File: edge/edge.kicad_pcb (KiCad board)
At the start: 2 copper layers, 50 x 50 mm, 22 parts, among them IC1 ATTINY861A-S, P1 CONN_6, P2 CONN_6, P3 CONN_5, P4 CONN_6, P5 CONN_3X2, Q1 MOSFET_N, Q2 MOSFET_N, Q3 MOSFET_N

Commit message: Last version before ATtiny24A
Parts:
- added R4: 10K, SM0603, F.Cu at (215.5, 112.5)
- added R5: 10K, SM0603, F.Cu at (217.5, 112.5)
- moved C5 20.2 mm to (211.0, 122.0), turned to 270 degrees
- moved C6 19.4 mm to (212.0, 115.0), turned to 90 degrees
- moved C8 17.5 mm to (212.0, 119.0), turned to 270 degrees
- moved P3 17.0 mm to (208.0, 141.0), turned to 90 degrees
- moved Q3 16.5 mm to (213.0, 130.0)
- moved R3 16.1 mm to (213.0, 127.0), turned to 0 degrees
- moved C2 15.7 mm to (219.5, 114.5), turned to 90 degrees
- moved C9 13.5 mm to (238.0, 107.0), turned to 90 degrees
- moved P4 13.3 mm to (229.5, 122.5), turned to 180 degrees
- moved P5 11.1 mm to (236.2, 121.0), turned to 90 degrees
- moved C4 10.3 mm to (221.5, 125.0)
- moved P1 10.0 mm to (208.0, 113.0)
- moved P2 10.0 mm to (242.0, 113.0)
- moved Q1 8.06 mm to (228.0, 130.0)
- moved C7 7.81 mm to (238.0, 111.0), turned to 270 degrees
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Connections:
- C3 pad 2: N-000007 (its old number) -> /OUT
- IC1 pad 1: /OUT -> /MOSI
- IC1 pad 19: N-0000019 (its old number) -> /BTN2
- IC1 pad 2: /RED -> /BLUE
- IC1 pad 20: /PA0 -> /BTN1
- IC1 pad 3: N-000004 -> /PB2
- IC1 pad 7: N-000005 -> /PB4
- IC1 pad 8: /BLUE -> /RED
- L1 pad 1: /OUT -> /MOSI
- L1 pad 2: N-000007 (its old number) -> /OUT
- P4 pad 5: /PA0 -> /PB2
- P4 pad 6: /PA2 -> /PB4
- P5 pad 1: /MISO -> /BLUE
- P5 pad 3: /SCK -> /PB2
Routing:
- net +3.3V: track 0.00 -> 101.2 mm, vias 0 -> 6
- net +12V: track 0.00 -> 93.2 mm, vias 0 -> 2
- net /OUT: track 0.00 -> 50.1 mm
- net N-000001: track 0.00 -> 35.6 mm
- net GND: track 0.00 -> 31.6 mm, vias 0 -> 12
- net /INCCW2: track 0.00 -> 25.6 mm, vias 0 -> 2
- net /INCW2: track 0.00 -> 24.6 mm
- net N-0000018: track 0.00 -> 22.4 mm
- net /\RESET: track 0.00 -> 21.6 mm
- net /INCCW1: track 0.00 -> 16.4 mm
- net /INCW1: track 0.00 -> 16.1 mm
- net N-0000019: track 0.00 -> 10.9 mm
- net /BLUE: track 0.00 -> 10.2 mm
- net /PB2: track 0.00 -> 10.1 mm
- net /PB4: track 0.00 -> 8.33 mm
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- added copper zone on F.Cu, net /BTN1C
- added copper zone on F.Cu, net /BTN2C
- added copper zone on B.Cu, net GND
- added copper zone on F.Cu, net GND
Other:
- net class Default: clearance 0.254 -> 0.2032; trace_width 0.254 -> 0.2032; via_dia 0.889 -> 0.6096; via_drill 0.635 -> 0.3048
- net class hipower added: clearance 0.3048, trace_width 0.508, via_dia 1.27, via_drill 0.762
- net class power added: clearance 0.2032, trace_width 0.3048, via_dia 0.889, via_drill 0.508
- rule trace_clearance: 0.254 -> 0.2032
- rule trace_min: 0.254 -> 0.1524
- rule via_min_drill: 0.508 -> 0.3048
- rule via_min_size: 0.889 -> 0.6096

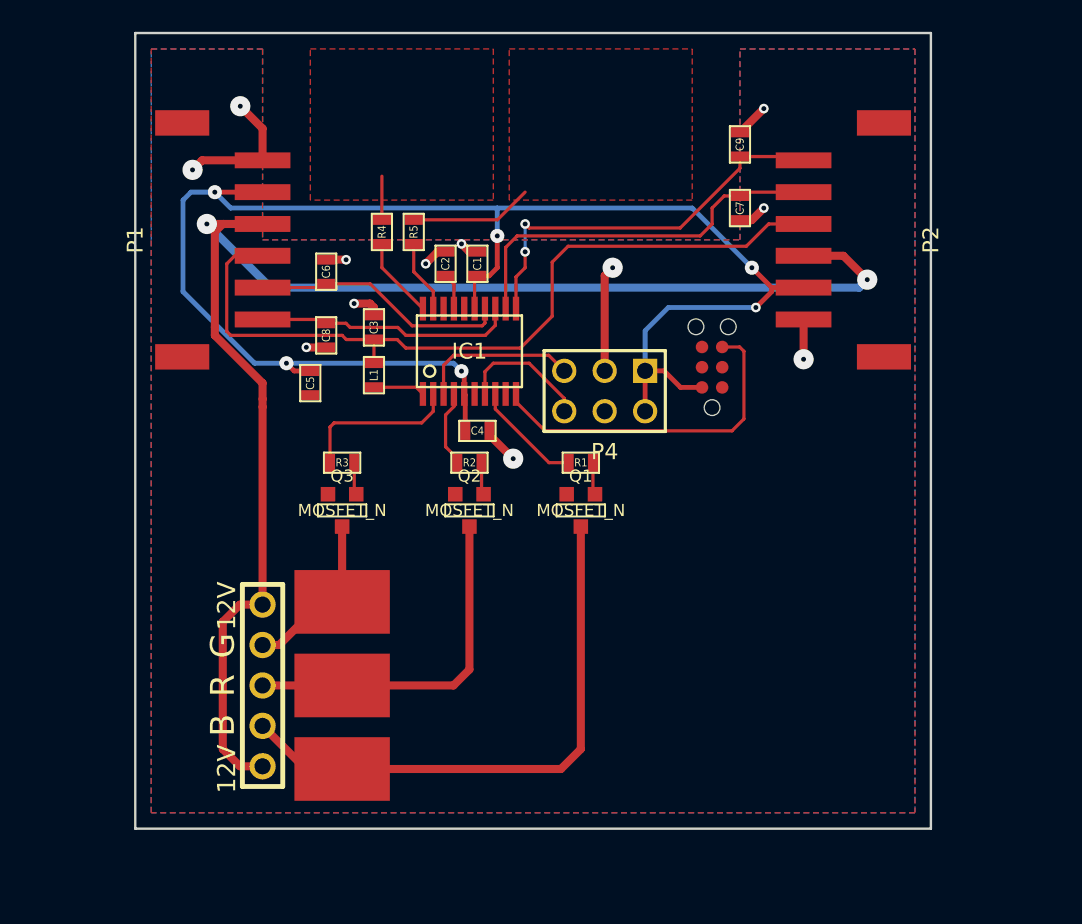
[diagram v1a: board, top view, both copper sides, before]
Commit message: ATtiny24A based edge board
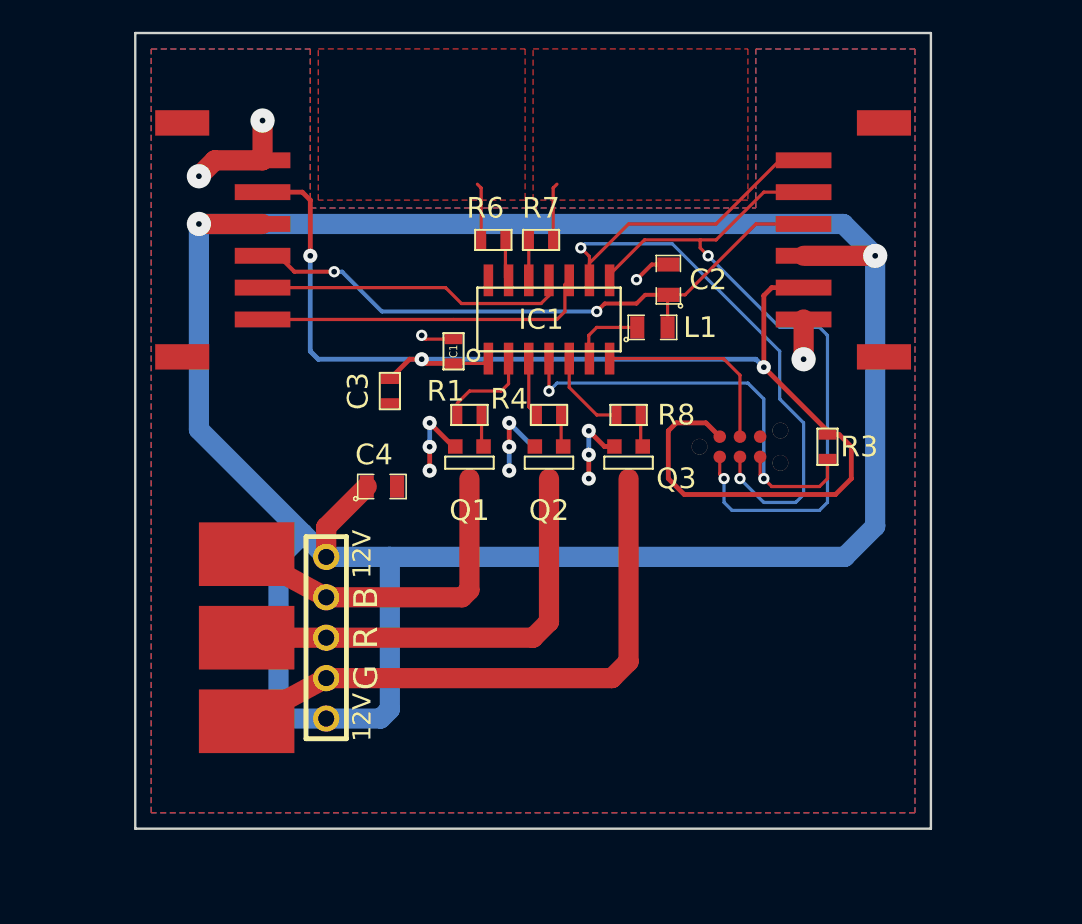
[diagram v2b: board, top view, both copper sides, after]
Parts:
- removed C5: 2.2uF, SM0603
- removed C6, C7, C8, C9: 0.1uF, SM0603
- removed P4: CONN_6, pin_array_3x2
- removed R2: 22R, SM0603
- removed R5: 10K, SM0603
- added R6: 10K, SM0603, F.Cu at (222.5, 113.0)
- added R7: 10K, SM0603, F.Cu at (225.5, 113.0)
- added R8: 170R, SM0603, F.Cu at (231.0, 124.0)
- C2, C4: value 0.1uF -> 10uF; footprint SM0603 -> SM0805
- C3: value 0.1uF -> 1uF
- IC1: value ATTINY861A-S -> ATTINY24A-SS; footprint TSSOP20-4.5MM -> SOIC14-4MM
- L1: footprint SM0603 -> SM0805
- Q1, Q2, Q3: value MOSFET_N -> NPN; footprint SOT23GDS -> SOT23EBC
- R1: value 22R -> 170R
- R3: value 22R -> 10K
- R4: value 10K -> 170R
- moved R3 30.5 mm to (243.5, 126.0), turned to 90 degrees
- moved Q3 18.2 mm to (231.0, 127.0)
- moved L1 17.8 mm to (232.5, 118.5), turned to 0 degrees
- moved R4 15.6 mm to (226.0, 124.0), turned to 0 degrees
- moved C2 14.0 mm to (233.5, 115.5)
- moved Q1 7.62 mm to (221.0, 127.0)
- moved R1 7.62 mm to (221.0, 124.0)
- moved C4 6.95 mm to (215.5, 128.5), turned to 0 degrees
- moved Q2 5.83 mm to (226.0, 127.0)
- moved C1 5.70 mm to (220.0, 120.0), turned to 270 degrees
- moved IC1 5.39 mm to (226.0, 118.0)
- moved P5 5.30 mm to (238.0, 126.0), turned to 0 degrees
- moved P3 5.00 mm to (212.0, 138.0), turned to 270 degrees
- moved C3 4.12 mm to (216.0, 122.5)
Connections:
- C1 pad 1: +3.3V -> GND
- C1 pad 2: GND -> +3.3V
- C2 pad 1: N-000006 -> /OUT
- C3 pad 1: GND -> +3.3V
- C3 pad 2: /OUT -> GND
- C4 pad 1: GND -> +12V
- C4 pad 2: +3.3V -> GND
- IC1 pad 1: /MOSI -> +3.3V
- IC1 pad 10: /\RESET -> /INCCW1
- IC1 pad 11: /INCCW2 -> /INCW1
- IC1 pad 12: /INCW2 -> /BTN2
- IC1 pad 13: /INCCW1 -> /BTN1
- IC1 pad 14: /INCW1 -> GND
- IC1 pad 2: /BLUE -> /RED
- IC1 pad 3: /PB2 -> /GREEN
- IC1 pad 4: /GREEN -> /\RESET
- IC1 pad 5: +3.3V -> /BLUE
- IC1 pad 6: GND -> N-0000010
- IC1 pad 7: /PB4 -> /MOSI
- IC1 pad 8: /RED -> /INCW2
- IC1 pad 9: N-000007 -> /INCCW2
- L1 pad 1: /MOSI -> N-0000010
- P3 pad 2: N-000001 -> /REDP
- P3 pad 3: N-0000018 -> /GREENP
- P3 pad 4: N-0000019 -> /BLUEP
- P5 pad 1: /BLUE -> /INCW2
- P5 pad 3: /PB2 -> /INCCW2
- R1 pad 2: N-0000015 -> /RB
- R3 pad 1: /BLUE -> /\RESET
- R3 pad 2: N-0000017 -> +3.3V
- R4 pad 1: /BTN1 -> /GREEN
- R4 pad 2: /BTN1C -> /GB
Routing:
- net +12V: track 93.2 -> 162.6 mm
- net /BLUEP: track 0.00 -> 36.6 mm
- net N-000001: track 35.6 -> 0.00 mm
- net /GREENP: track 0.00 -> 28.4 mm
- net /INCCW2: track 25.6 -> 50.7 mm
- net N-0000018: track 22.4 -> 0.00 mm
- net /REDP: track 0.00 -> 21.9 mm
- net /INCW2: track 24.6 -> 45.9 mm, vias 0 -> 2
- net +3.3V: track 101.2 -> 84.6 mm, vias 6 -> 3
- net N-0000019: track 10.9 -> 0.00 mm
- net /OUT: track 50.1 -> 39.8 mm, vias 0 -> 2
- net /PB2: track 10.1 -> 0.00 mm
- net /MOSI: track 3.25 -> 12.5 mm
- net /PB4: track 8.33 -> 0.00 mm
- net GND: track 31.6 -> 24.2 mm, vias 12 -> 11
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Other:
- net class Default: via_dia 0.6096 -> 0.7112; via_drill 0.3048 -> 0.3556
- net class hipower: clearance 0.3048 -> 0.508; trace_width 0.508 -> 1.27; via_dia 1.27 -> 1.524

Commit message: Game of Life edge board rerouting
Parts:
- added C5: C, SM0603, F.Cu at (219.5, 113.0)
- added C6: C, SM0603, F.Cu at (228.6, 112.0)
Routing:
- net +12V: track 162.6 -> 290.6 mm, vias 2 -> 4
- net GND: track 24.2 -> 46.1 mm, vias 11 -> 15
- net /BTN2C: track 3.60 -> 5.28 mm
- net /BTN1C: track 3.60 -> 5.13 mm

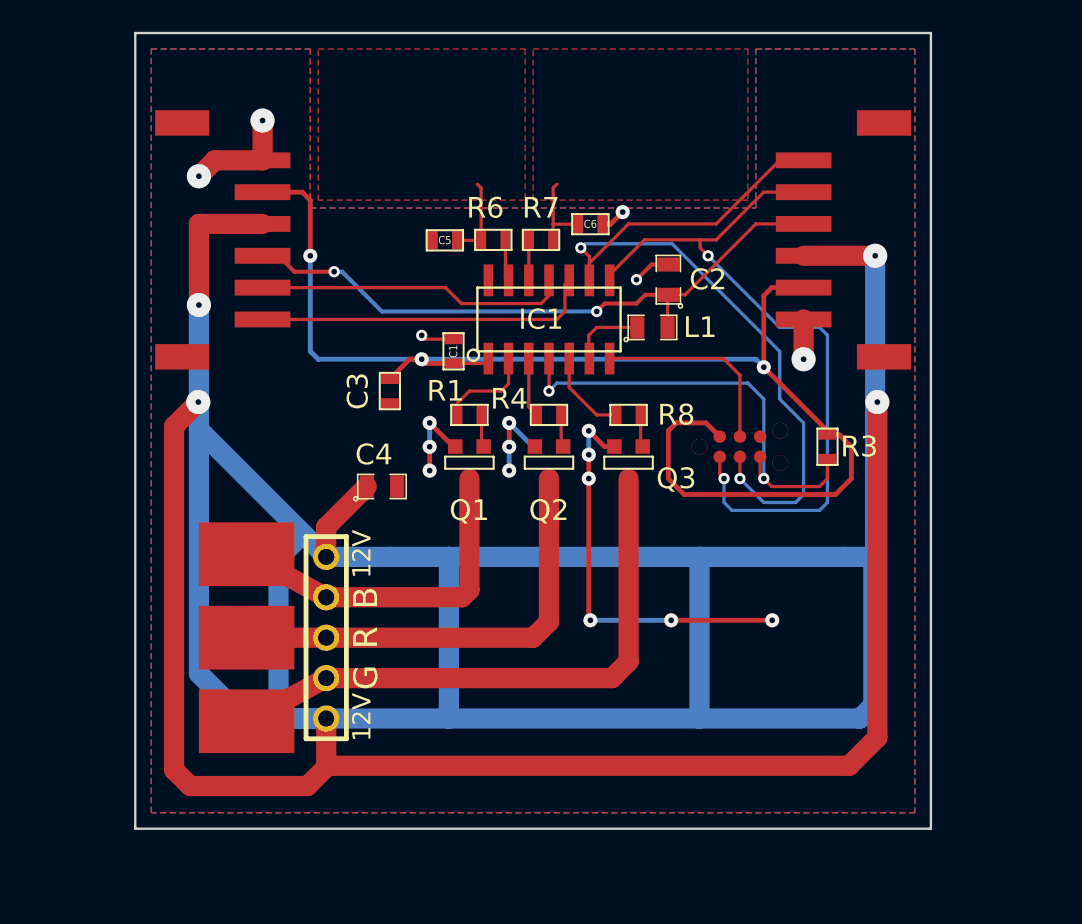
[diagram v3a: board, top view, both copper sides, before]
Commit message: Only one cap button, add LED to Game of Life edge boards
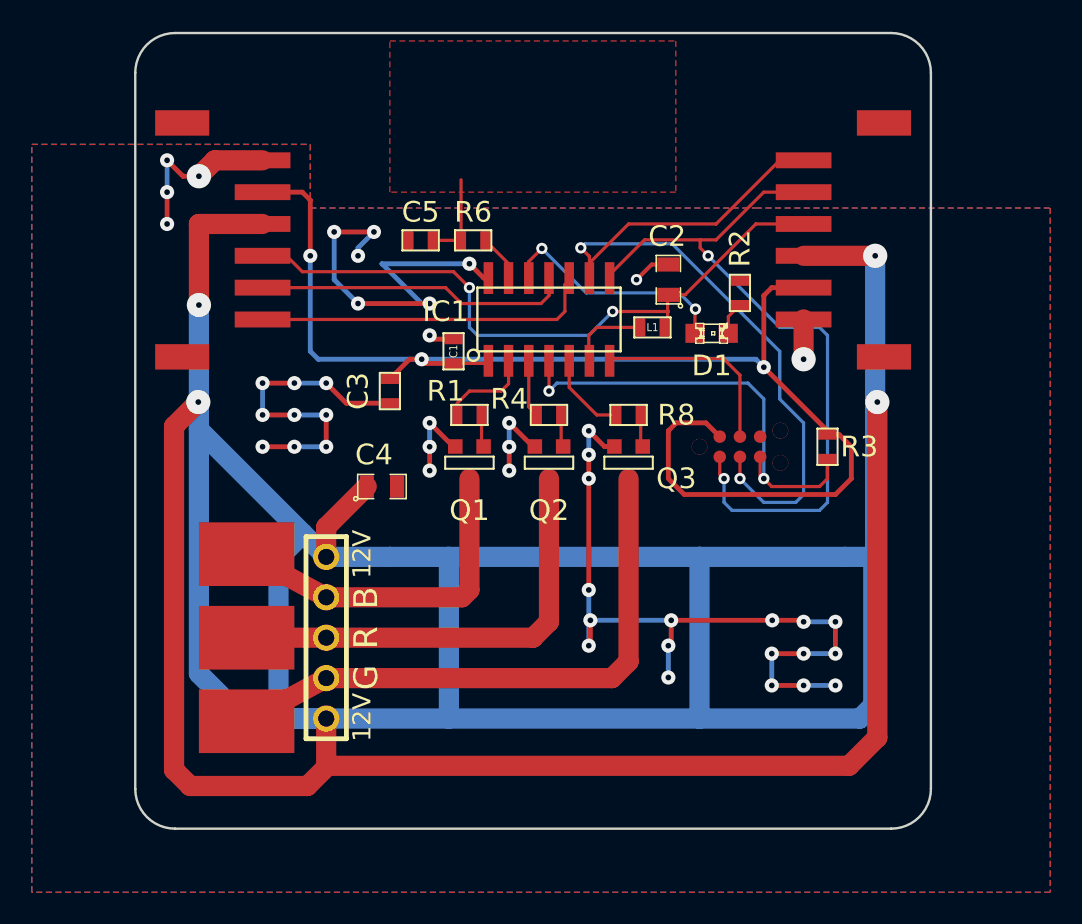
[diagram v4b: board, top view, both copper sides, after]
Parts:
- removed C6: C, SM0603
- removed R7: 10K, SM0603
- added D1: LED, LED-0805, F.Cu at (236.2, 118.9)
- added R2: 1K, SM0603, F.Cu at (238.0, 116.3)
- L1: footprint SM0805 -> SM0603
- moved C5 1.52 mm to (217.9, 113.0)
- moved R6 1.27 mm to (221.2, 113.0)
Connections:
- C5 pad 2: GND -> N-0000014
- IC1 pad 12: /BTN2 -> /LED1
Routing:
- net GND: track 46.1 -> 121.7 mm, vias 15 -> 46
- net /LED1: track 0.00 -> 15.1 mm, vias 0 -> 2
- net /BTN2C: track 5.28 -> 0.00 mm
- net (no net): track 5.12 -> 0.00 mm, vias 3 -> 0
- net /BTN2: track 2.54 -> 0.00 mm
- net /OUT: track 39.8 -> 42.1 mm
- net N-0000017: track 0.00 -> 2.08 mm
- removed copper zone on F.Cu, net /BTN2C
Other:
- outline, holes or cut-outs redrawn
